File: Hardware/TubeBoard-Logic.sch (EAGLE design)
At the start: 33 parts, among them IC1 74HC373DW, IC2 74HC373DW, IC3 74HC85D, IC4 74HC08D, IC5 74HC04D, IC6 MKE04Z8, IC7 74HC139D, IC8 74HC373DW, J1 CORTEX_DEBUG_PTH

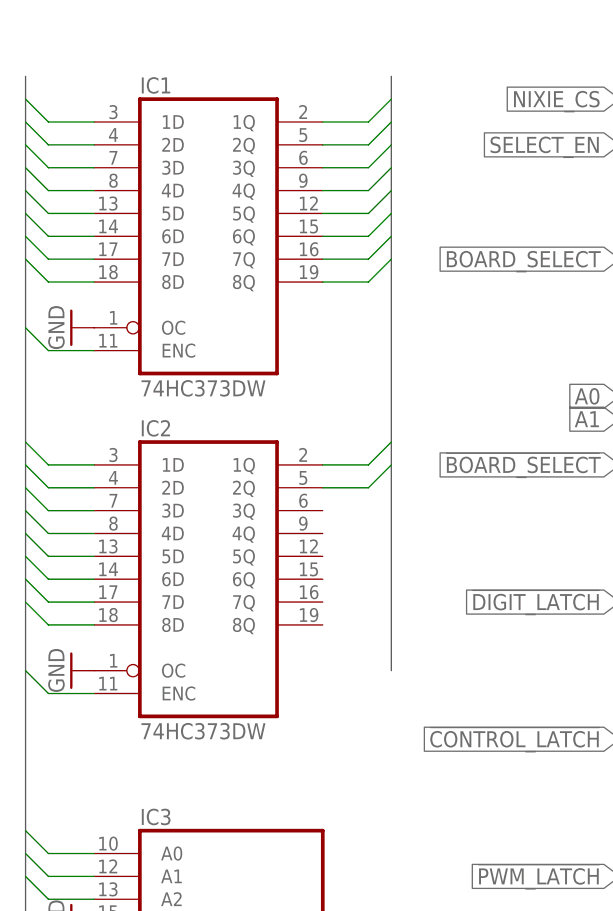
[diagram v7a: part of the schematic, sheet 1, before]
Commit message: more routing of tube logic board
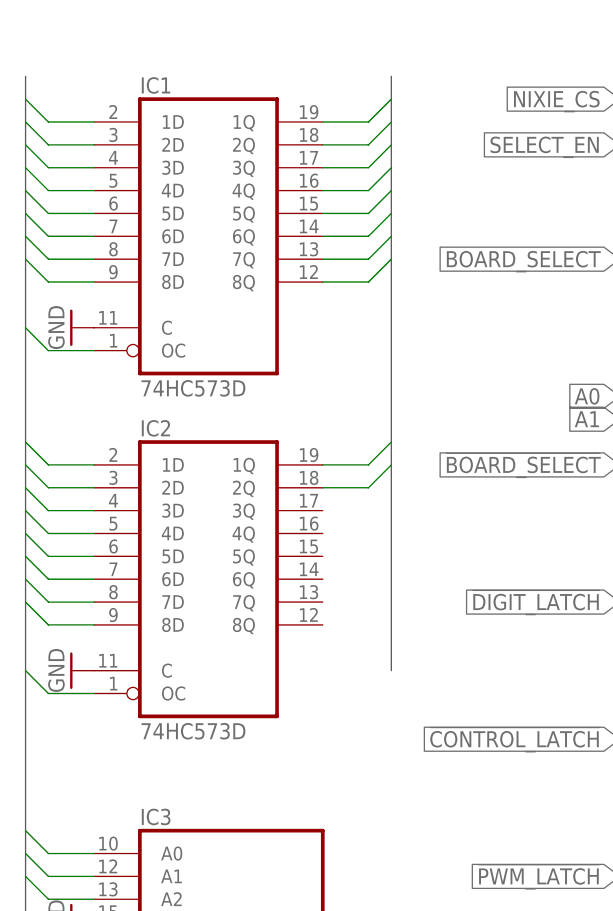
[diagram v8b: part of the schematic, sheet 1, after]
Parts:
- IC1, IC2, IC8: value 74HC373DW -> 74HC573D; device 74xx-eu:74HC373DW -> 74xx-eu:74HC573D
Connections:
- net CONTROL_LATCH: now also IC2A.OC; no longer IC2A.ENC
- net DIGIT_LATCH: now also IC1A.OC; no longer IC1A.ENC
- net GND: now also IC1A.C, IC2A.C, IC8A.C; no longer IC1A.OC, IC2A.OC, IC8A.OC
- net PWM_D0: now also IC6.PB7; no longer IC6.PB4
- net PWM_D1: now also IC6.PB6; no longer IC6.PB5
- net PWM_D2: now also IC6.PB5; no longer IC6.PB6
- net PWM_D3: now also IC6.PB4; no longer IC6.PB7
- net PWM_LATCH: now also IC8A.OC; no longer IC8A.ENC
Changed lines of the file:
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@@
 <?xml version="1.0" encoding="utf-8"?>
 <!DOCTYPE eagle SYSTEM "eagle.dtd">
-<eagle version="9.2.1">
+<eagle version="9.3.2">
 <drawing>
 <settings>
@@
 <part name="P+5" library="supply1" library_urn="urn:adsk.eagle:library:371" deviceset="+5V" device=""/>
 <part name="GND12" library="supply1" library_urn="urn:adsk.eagle:library:371" deviceset="GND" device=""/>
-<part name="IC1" library="74xx-eu" library_urn="urn:adsk.eagle:library:85" deviceset="74*373" device="DW" package3d_urn="urn:adsk.eagle:package:2018/1" technology="HC"/>
+<part name="IC1" library="74xx-eu" library_urn="urn:adsk.eagle:library:85" deviceset="74*573" device="D" package3d_urn="urn:adsk.eagle:package:2018/2" technology="HC"/>
 <part name="P+7" library="supply1" library_urn="urn:adsk.eagle:library:371" deviceset="+5V" device=""/>
 <part name="GND14" library="supply1" library_urn="urn:adsk.eagle:library:371" deviceset="GND" device=""/>
 <part name="GND1" library="supply1" library_urn="urn:adsk.eagle:library:371" deviceset="GND" device=""/>
-<part name="IC2" library="74xx-eu" library_urn="urn:adsk.eagle:library:85" deviceset="74*373" device="DW" package3d_urn="urn:adsk.eagle:package:2018/1" technology="HC"/>
+<part name="IC2" library="74xx-eu" library_urn="urn:adsk.eagle:library:85" deviceset="74*573" device="D" package3d_urn="urn:adsk.eagle:package:2018/2" technology="HC"/>
 <part name="GND2" library="supply1" library_urn="urn:adsk.eagle:library:371" deviceset="GND" device=""/>
 <part name="IC3" library="74xx-eu" library_urn="urn:adsk.eagle:library:85" deviceset="74*85" device="D" package3d_urn="urn:adsk.eagle:package:2010/1" technology="HC">
@@
 <part name="GND6" library="supply1" library_urn="urn:adsk.eagle:library:371" deviceset="GND" device=""/>
 <part name="P+1" library="supply1" library_urn="urn:adsk.eagle:library:371" deviceset="+5V" device=""/>
-<part name="IC5" library="74xx-eu" library_urn="urn:adsk.eagle:library:85" deviceset="74*04" device="D" package3d_urn="urn:adsk.eagle:package:2007/1" technology="HC"/>
-<part name="IC4" library="74xx-eu" library_urn="urn:adsk.eagle:library:85" deviceset="74*08" device="D" package3d_urn="urn:adsk.eagle:package:2007/1" technology="HC"/>
+<part name="IC5" library="74xx-eu" library_urn="urn:adsk.eagle:library:85" deviceset="74*04" device="D" package3d_urn="urn:adsk.eagle:package:1010/2" technology="HC"/>
+<part name="IC4" library="74xx-eu" library_urn="urn:adsk.eagle:library:85" deviceset="74*08" device="D" package3d_urn="urn:adsk.eagle:package:1010/2" technology="HC"/>
 <part name="C3" library="rcl" library_urn="urn:adsk.eagle:library:334" deviceset="C-EU" device="C1206" package3d_urn="urn:adsk.eagle:package:23618/2" value="100nF"/>
 <part name="S1" library="switch-dil" library_urn="urn:adsk.eagle:library:375" deviceset="SD4-03" device="" package3d_urn="urn:adsk.eagle:package:27238/1">
@@
 <attribute name="MOUSER" value="771-HC139D652"/>
 </part>
-<part name="IC8" library="74xx-eu" library_urn="urn:adsk.eagle:library:85" deviceset="74*373" device="DW" package3d_urn="urn:adsk.eagle:package:2018/1" technology="HC"/>
+<part name="IC8" library="74xx-eu" library_urn="urn:adsk.eagle:library:85" deviceset="74*573" device="D" package3d_urn="urn:adsk.eagle:package:2018/2" technology="HC"/>
 <part name="GND25" library="supply1" library_urn="urn:adsk.eagle:library:371" deviceset="GND" device=""/>
 <part name="C9" library="rcl" library_urn="urn:adsk.eagle:library:334" deviceset="C-EU" device="C1206" package3d_urn="urn:adsk.eagle:package:23618/2" value="100nF"/>
@@
 </segment>
 <segment>
-<pinref part="IC1" gate="A" pin="OC"/>
+<pinref part="IC1" gate="A" pin="C"/>
 <pinref part="GND1" gate="1" pin="GND"/>
 </segment>
 <segment>
-<pinref part="IC2" gate="A" pin="OC"/>
+<pinref part="IC2" gate="A" pin="C"/>
 <pinref part="GND2" gate="1" pin="GND"/>
 </segment>
@@
 <net name="DIGIT_LATCH" class="0">
 <segment>
-<pinref part="IC1" gate="A" pin="ENC"/>
+<pinref part="IC1" gate="A" pin="OC"/>
 <wire x1="15.24" y1="142.24" x2="10.16" y2="142.24" width="0.1524" layer="91"/>
 <wire x1="10.16" y1="142.24" x2="7.62" y2="144.78" width="0.1524" layer="91"/>
@@
 <net name="CONTROL_LATCH" class="0">
 <segment>
-<pinref part="IC2" gate="A" pin="ENC"/>
+<pinref part="IC2" gate="A" pin="OC"/>
 <wire x1="15.24" y1="104.14" x2="10.16" y2="104.14" width="0.1524" layer="91"/>
 <wire x1="10.16" y1="104.14" x2="7.62" y2="106.68" width="0.1524" layer="91"/>
@@
 </segment>
 <segment>
-<pinref part="IC8" gate="A" pin="OC"/>
+<pinref part="IC8" gate="A" pin="C"/>
 <pinref part="GND25" gate="1" pin="GND"/>
 </segment>
@@
 <net name="PWM_D3" class="0">
 <segment>
+<pinref part="IC8" gate="A" pin="4Q"/>
+<wire x1="43.18" y1="104.14" x2="48.26" y2="104.14" width="0.1524" layer="91"/>
+<label x="48.26" y="104.14" size="1.778" layer="95" xref="yes"/>
+</segment>
+<segment>
+<pinref part="IC6" gate="G$1" pin="PB4"/>
+<wire x1="109.22" y1="27.94" x2="114.3" y2="27.94" width="0.1524" layer="91"/>
+<label x="114.3" y="27.94" size="1.778" layer="95" xref="yes"/>
+</segment>
+</net>
+<net name="PWM_D2" class="0">
+<segment>
+<pinref part="IC8" gate="A" pin="3Q"/>
+<wire x1="43.18" y1="106.68" x2="48.26" y2="106.68" width="0.1524" layer="91"/>
+<label x="48.26" y="106.68" size="1.778" layer="95" xref="yes"/>
+</segment>
+<segment>
+<pinref part="IC6" gate="G$1" pin="PB5"/>
+<wire x1="109.22" y1="25.4" x2="114.3" y2="25.4" width="0.1524" layer="91"/>
+<label x="114.3" y="25.4" size="1.778" layer="95" xref="yes"/>
+</segment>
+</net>
+<net name="PWM_D1" class="0">
+<segment>
+<pinref part="IC8" gate="A" pin="2Q"/>
+<wire x1="43.18" y1="109.22" x2="48.26" y2="109.22" width="0.1524" layer="91"/>
+<label x="48.26" y="109.22" size="1.778" layer="95" xref="yes"/>
+</segment>
+<segment>
+<pinref part="IC6" gate="G$1" pin="PB6"/>
+<wire x1="109.22" y1="22.86" x2="114.3" y2="22.86" width="0.1524" layer="91"/>
+<label x="114.3" y="22.86" size="1.778" layer="95" xref="yes"/>
+</segment>
+</net>
+<net name="PWM_D0" class="0">
+<segment>
+<pinref part="IC8" gate="A" pin="1Q"/>
+<wire x1="43.18" y1="111.76" x2="48.26" y2="111.76" width="0.1524" layer="91"/>
+<label x="48.26" y="111.76" size="1.778" layer="95" xref="yes"/>
+</segment>
+<segment>
 <pinref part="IC6" gate="G$1" pin="PB7"/>
 <wire x1="109.22" y1="20.32" x2="114.3" y2="20.32" width="0.1524" layer="91"/>
 <label x="114.3" y="20.32" size="1.778" layer="95" xref="yes"/>
-</segment>
-<segment>
-<pinref part="IC8" gate="A" pin="4Q"/>
-<wire x1="43.18" y1="104.14" x2="48.26" y2="104.14" width="0.1524" layer="91"/>
-<label x="48.26" y="104.14" size="1.778" layer="95" xref="yes"/>
-</segment>
-</net>
-<net name="PWM_D2" class="0">
-<segment>
-<pinref part="IC6" gate="G$1" pin="PB6"/>
-<wire x1="109.22" y1="22.86" x2="114.3" y2="22.86" width="0.1524" layer="91"/>
-<label x="114.3" y="22.86" size="1.778" layer="95" xref="yes"/>
-</segment>
-<segment>
-<pinref part="IC8" gate="A" pin="3Q"/>
-<wire x1="43.18" y1="106.68" x2="48.26" y2="106.68" width="0.1524" layer="91"/>
-<label x="48.26" y="106.68" size="1.778" layer="95" xref="yes"/>
-</segment>
-</net>
-<net name="PWM_D1" class="0">
-<segment>
-<pinref part="IC6" gate="G$1" pin="PB5"/>
-<wire x1="109.22" y1="25.4" x2="114.3" y2="25.4" width="0.1524" layer="91"/>
-<label x="114.3" y="25.4" size="1.778" layer="95" xref="yes"/>
-</segment>
-<segment>
-<pinref part="IC8" gate="A" pin="2Q"/>
-<wire x1="43.18" y1="109.22" x2="48.26" y2="109.22" width="0.1524" layer="91"/>
-<label x="48.26" y="109.22" size="1.778" layer="95" xref="yes"/>
-</segment>
-</net>
-<net name="PWM_D0" class="0">
-<segment>
-<pinref part="IC6" gate="G$1" pin="PB4"/>
-<wire x1="109.22" y1="27.94" x2="114.3" y2="27.94" width="0.1524" layer="91"/>
-<label x="114.3" y="27.94" size="1.778" layer="95" xref="yes"/>
-</segment>
-<segment>
-<pinref part="IC8" gate="A" pin="1Q"/>
-<wire x1="43.18" y1="111.76" x2="48.26" y2="111.76" width="0.1524" layer="91"/>
-<label x="48.26" y="111.76" size="1.778" layer="95" xref="yes"/>
 </segment>
 </net>
@@
 <net name="PWM_LATCH" class="0">
 <segment>
-<pinref part="IC8" gate="A" pin="ENC"/>
+<pinref part="IC8" gate="A" pin="OC"/>
 <wire x1="17.78" y1="86.36" x2="12.7" y2="86.36" width="0.1524" layer="91"/>
 <wire x1="12.7" y1="86.36" x2="10.16" y2="88.9" width="0.1524" layer="91"/>
